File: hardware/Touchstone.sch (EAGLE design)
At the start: 76 parts, among them J3 USB-MICROB, U1 NEOPIXEL_NANO_2427, U10 TSL2591, U11 915MHz, U12 MH-Z19, U13 CCS811-I2C, U14 IAQ-CORE-C, U15 VLP-450-F, U16 VLP-450-F, U2 FT231XQ-R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

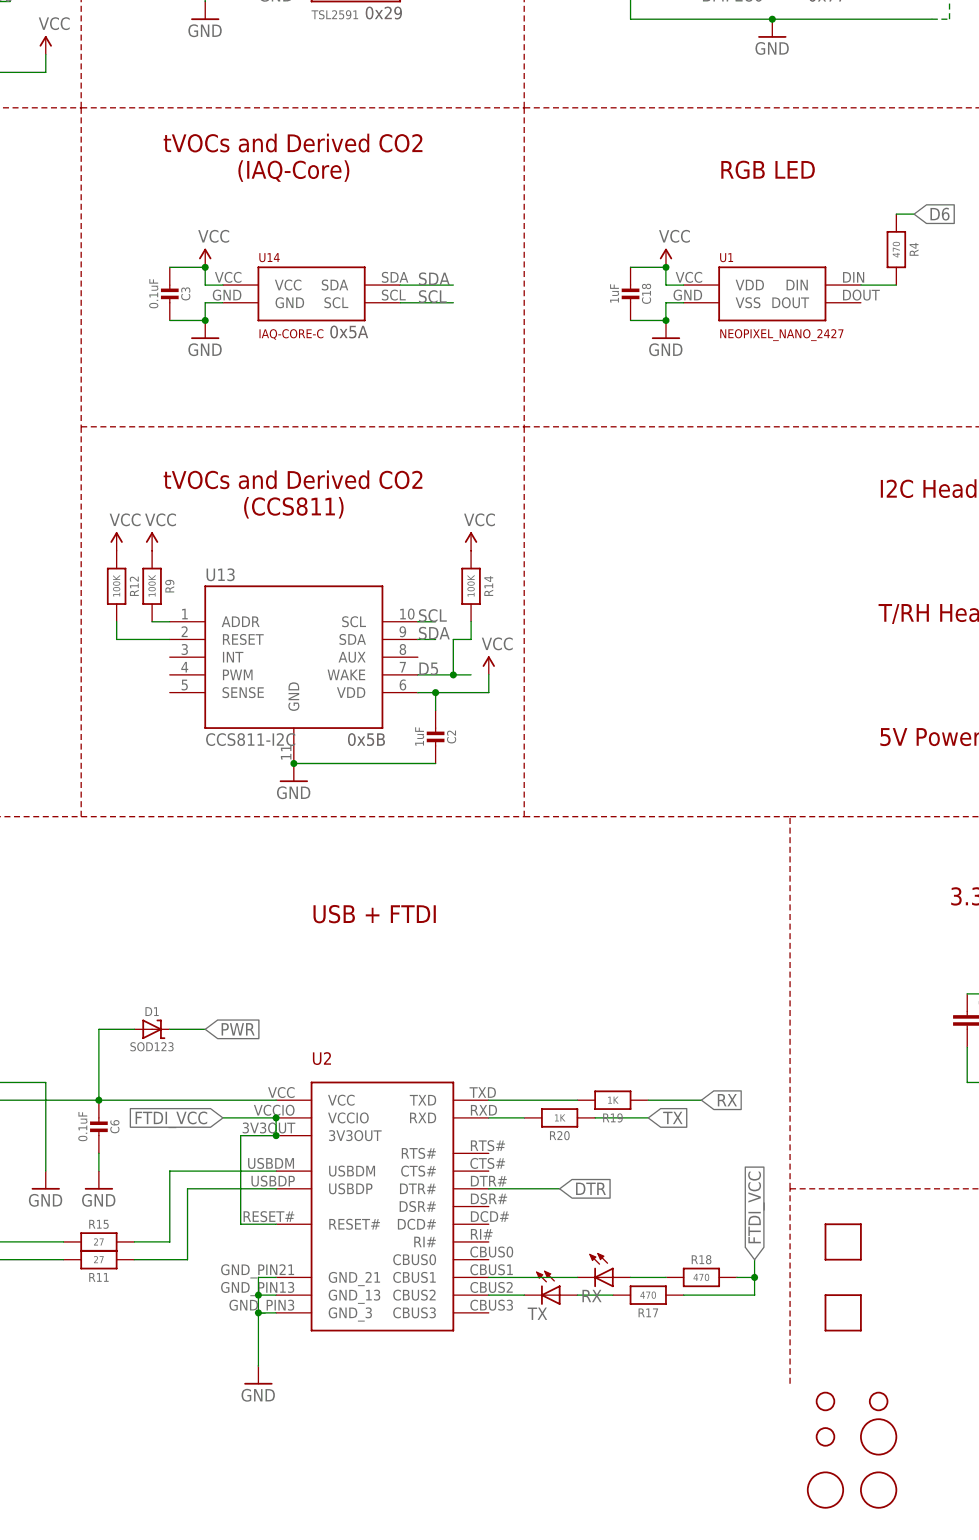
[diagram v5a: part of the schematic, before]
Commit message: Added another fiducial marker
- rearranged fiducials a bit
- minor schematic update
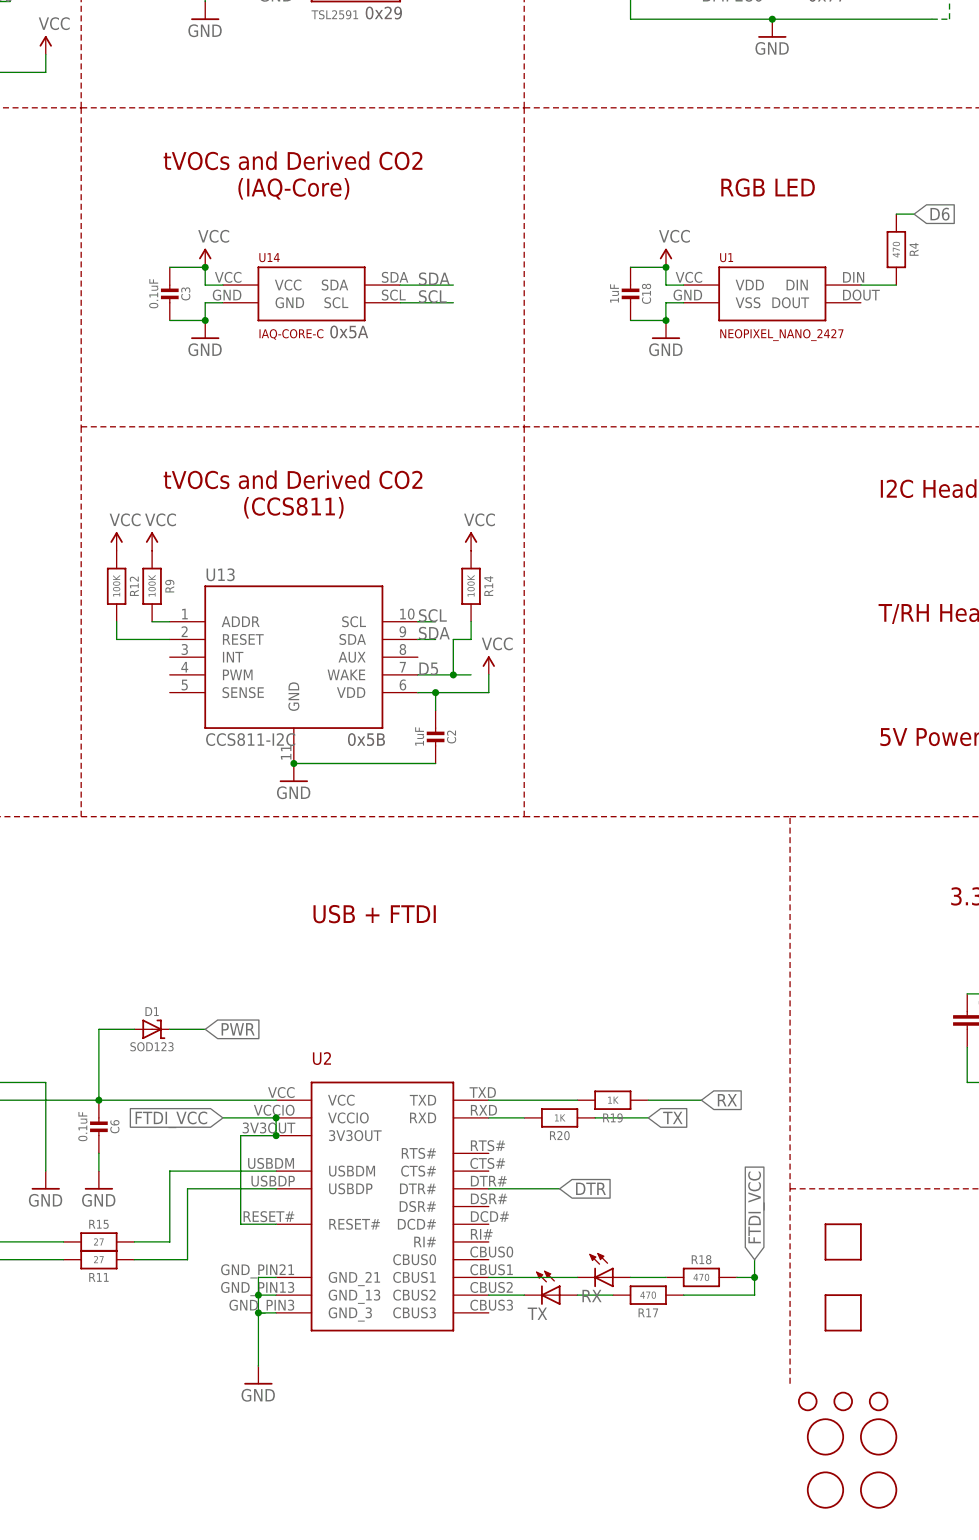
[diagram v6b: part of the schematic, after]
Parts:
- added U$7: FIDUCIAL, adafruit:FIDUCIAL
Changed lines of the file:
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@@
 <part name="SUPPLY21" library="SparkFun-Aesthetics" deviceset="VCC" device=""/>
 <part name="GND15" library="SparkFun-Aesthetics" deviceset="GND" device=""/>
+<part name="U$7" library="adafruit" deviceset="FIDUCIAL" device=""/>
 </parts>
 <sheets>
@@
 <plain>
 <text x="134.62" y="129.54" size="2.54" layer="94" font="vector">Light Intensity</text>
-<text x="147.32" y="78.74" size="2.54" layer="94" font="vector" align="bottom-center">tVOCs and Derived CO2
+<text x="147.32" y="76.2" size="2.54" layer="94" font="vector" align="bottom-center">tVOCs and Derived CO2
 (IAQ-Core)</text>
 <text x="203.2" y="129.54" size="2.54" layer="94" font="vector">Air Pressure</text>
@@
 <text x="248.666" y="-87.122" size="2.54" layer="94" font="vector" ratio="10">github.crtlabs.org</text>
 <text x="157.48" y="101.6" size="1.778" layer="97">0x29</text>
-<text x="208.28" y="78.74" size="2.54" layer="94" font="vector">RGB LED</text>
+<text x="208.28" y="76.2" size="2.54" layer="94" font="vector">RGB LED</text>
 <text x="231.14" y="33.02" size="2.54" layer="94" font="vector">I2C Headers</text>
 <text x="73.66" y="129.54" size="2.54" layer="94" font="vector">PM2.5 sensor</text>
@@
 <instance part="SUPPLY10" gate="G$1" x="195.58" y="121.92"/>
 <instance part="SUPPLY12" gate="G$1" x="241.3" y="121.92"/>
-<instance part="H1" gate="G$1" x="223.52" y="-101.6"/>
+<instance part="H1" gate="G$1" x="220.98" y="-96.52"/>
 <instance part="H2" gate="G$1" x="231.14" y="-96.52"/>
 <instance part="FRAME1" gate="G$1" x="-71.12" y="-116.84"/>
@@
 <instance part="GND5" gate="1" x="302.26" y="50.8"/>
 <instance part="SUPPLY3" gate="G$1" x="264.16" y="78.74"/>
-<instance part="H3" gate="G$1" x="223.52" y="-96.52"/>
+<instance part="H3" gate="G$1" x="226.06" y="-96.52"/>
 <instance part="TC1" gate="A" x="-35.56" y="109.22" rot="R180"/>
 <instance part="U4" gate="G$1" x="27.94" y="109.22"/>
@@
 <instance part="SUPPLY21" gate="G$1" x="63.5" y="-43.18"/>
 <instance part="GND15" gate="1" x="63.5" y="-76.2"/>
+<instance part="U$7" gate="G$1" x="223.52" y="-101.6"/>
 </instances>
 <busses>

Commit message: v0.5.7 - updated sound level circuit
- Replaced MEMS mic with mini electret mic
- Added analog circuitry for the mic
- Some routing and silkscreen adjustments
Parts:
- removed C10: 4.7uF, Adafruit Feather 32u4 Bluefruit LE:MICROBUILDER_CAP_CERAMIC_0402MP
- removed C13: 0.1uF, Adafruit Feather 32u4 Bluefruit LE:MICROBUILDER_CAP_CERAMIC_0402MP
- removed C14: 1uF, Adafruit Feather 32u4 Bluefruit LE:MICROBUILDER_CAP_CERAMIC_0402MP
- removed C21: 100pF, Adafruit Feather 32u4 Bluefruit LE:MICROBUILDER_CAP_CERAMIC_0402MP
- removed R1, R2: 10K, Adafruit Feather 32u4 Bluefruit LE:MICROBUILDER_RESISTOR_0402MP
- removed R3: 1.5K, SparkFun-Passives:RESISTOR0805-RES
- removed R8: 100K, SparkFun-Passives:RESISTOR0805-RES
- removed U3: OPA344, SparkFun-AnalogIC:OPA344
- removed U6: ADMP401, SparkFun-Sensors:ADMP401
- added C22, C9: 10uF, Adafruit Feather 32u4 Bluefruit LE:MICROBUILDER_CAP_CERAMIC_0402MP
- added C23, C24: 1uF, Adafruit Feather 32u4 Bluefruit LE:MICROBUILDER_CAP_CERAMIC_0402MP
- added D3, D4: 120mA/40V/370mV, SparkFun-DiscreteSemi:DIODE-SCHOTTKY-RB751S40
- added MK1: MIC2-PTH, CMC-4015-40P:MIC2-PTH
- added R22, R27: 1K, Adafruit PowerBoost 1000C Rev B:MICROBUILDER_RESISTOR_0402MP
- added R23: 2.2K, Adafruit PowerBoost 1000C Rev B:MICROBUILDER_RESISTOR_0402MP
- added R24: 470K, Adafruit PowerBoost 1000C Rev B:MICROBUILDER_RESISTOR_0402MP
- added R25, R32: 100, Adafruit PowerBoost 1000C Rev B:MICROBUILDER_RESISTOR_0402MP
- added R26, R28, R29, R30: 10K, Adafruit PowerBoost 1000C Rev B:MICROBUILDER_RESISTOR_0402MP
- added R31: 22K, Adafruit PowerBoost 1000C Rev B:MICROBUILDER_RESISTOR_0402MP
- added U17: LMV324QT, LMV324:LMV324QT
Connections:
- removed net N$10: C21.1, R3.1, R8.2, U3.-IN
- removed net N$11: C14.1, R1.1, R2.2, U3.+IN
- removed net OUT: C10.2, U6.OUT
- new net AMP: C24.1, R24.2, U17G$1.OUT
- new net N$12: R22.2, R24.1, U17G$1.-IN
- new net N$14: D3.C, D4.C, R25.1, R31.1
- new net N$15: R27.2, U17G$3.-IN
- new net N$19: C24.2, R30.2
- new net N$20: C22.2, R25.2, R26.2, U17G$3.+IN
- new net N$21: D4.A, U17G$2.OUT
- new net N$22: D3.A, R30.1, R31.2, U17G$2.-IN
- new net N$8: C9.2, R22.1
- new net VCC/2: R28.2, R29.1, U17G$1.+IN
- new net _OUT: R27.1, R32.2, U17G$3.OUT
- net A0: now also R32.1; no longer C21.2, R8.1, U3.OUT
- net GND: now also C22.1, C23.1, MK1.2, R26.1, R28.1, U17G$1.-V, U17G$2.+IN; no longer C13.1, C14.2, R2.1, U3.V-, U6.GND@2, U6.GND@4, U6.GND@6
- net N$9: now also C9.1, MK1.1, R23.1; no longer C10.1, R3.2
- net VCC: now also C23.2, R23.2, R29.2, U17G$1.+V; no longer C13.2, R1.2, U3.V+, U6.VDD
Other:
- note added: "47K = low gain 100K = default gain 470K = high gain"
- moved on the sheet: R10, U7
